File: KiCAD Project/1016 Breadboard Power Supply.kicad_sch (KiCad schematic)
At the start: 0 parts

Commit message: V1.0.0.0
Final version 1, sent for fabrication.
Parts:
- added FID1, FID2, FID3: Fiducial, Fiducial:Fiducial_1mm_Mask2mm, symbol Mechanical:Fiducial
- added H1, H2, H3, H4: MountingHole, MountingHole:MountingHole_2.1mm, symbol Mechanical:MountingHole
- added P1: DW_PCB_Logo, DW_Footprint:DW_PCB_Logo, symbol DW_Library:DW_PCB_Logo
- added P2, P3: Solder_Stencil_Alignment_Pin, DW_Footprint:Solder_Stencil_Alignment_Pin, symbol DW_Library:Solder_Stencil_Alignment_Pin
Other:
- added sheet MCU Control (MCU Control.kicad_sch)
- added sheet Rail B Power Regulator (Rail B Power Regulator.kicad_sch)
- added sheet Rail Output (Rail Output.kicad_sch)
- added sheet Rail T Power Regulator (Rail T Power Regulator.kicad_sch)
- sheet MCU Power Regulator ports: added Vmcu; removed none

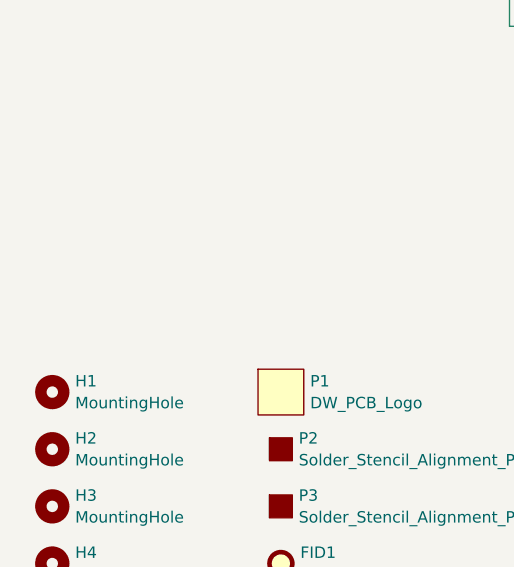
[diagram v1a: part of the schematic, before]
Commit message: v2.0.0.0
1016 Breadboard Power Supply v2

- Change FSW connection to the Vout on all regulators
- Change regulator to TPS62130A so that PG pin goes low on thermal shutdown and UVLO
- Change PG pullup to be a resistor at the regulator vice pullup within STM32 so that it can be actively discharged
- Remove resistor across rail outputs for discharging to improve efficiency
- Change board dimensions to correct span
- Change pinout of STM32 for better routing
- Change Tag-Connect footprint to momentary connection (no legs)
- Make sure Tag-Connect footprint doesn't have solder paste layer
- Added heat sinks on bottom under rail regulators, added thermal vias
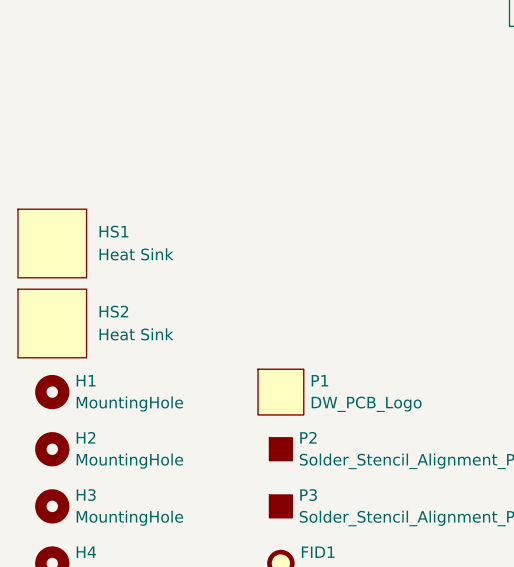
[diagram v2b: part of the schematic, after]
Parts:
- added HS1, HS2: Heat Sink, 1016:HSB01-080808, symbol 1016:HSB01-080808
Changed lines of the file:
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@@
+    )
+  )
+  (symbol (lib_id "1016:HSB01-080808") (at 38.1 148.59 0) (unit 1)
+    (in_bom yes) (on_board yes) (dnp no)
+    (property "Reference" "HS1" (at 43.18 147.32 0)
+      (effects (font (size 1.27 1.27)) (justify left))
+    )
+    (property "Value" "Heat Sink" (at 43.18 149.86 0)
+      (effects (font (size 1.27 1.27)) (justify left))
+    )
+    (property "Footprint" "1016:HSB01-080808" (at 38.1 156.21 0)
+      (effects (font (size 1.27 1.27)) hide)
+    )
+    (property "Datasheet" "https://www.mouser.com/datasheet/2/670/hsb01_080808-2449749.pdf" (at 38.1 140.97 0)
+      (effects (font (size 1.27 1.27)) hide)
+    )
+    (property "Description" "Heat Sink" (at 38.1 148.59 0)
+      (effects (font (size 1.27 1.27)) hide)
+    )
+    (property "Height" "8" (at 38.1 148.59 0)
+      (effects (font (size 1.27 1.27)) hide)
+    )
+    (property "Manufacturer_Name" "CUI Devices" (at 38.1 148.59 0)
+      (effects (font (size 1.27 1.27)) hide)
+    )
+    (property "Manufacturer_Part_Number" "HSB01-080808" (at 38.1 148.59 0)
+      (effects (font (size 1.27 1.27)) hide)
+    )
+    (property "Mouser Part Number" "490-HSB01-080808" (at 38.1 148.59 0)
+      (effects (font (size 1.27 1.27)) hide)
+    )
+    (property "Spec" "8.5mm x 8.5mm Al" (at 38.1 148.59 0)
+      (effects (font (size 1.27 1.27)) hide)
+    )
+    (instances
+      (project "1016 Breadboard Power Supply"
+        (path "/f4b22203-0926-4e3a-b453-85f22789c08a"
+          (reference "HS1") (unit 1)
+        )
+      )
+    )
+  )
+  (symbol (lib_id "1016:HSB01-080808") (at 38.1 157.48 0) (unit 1)
+    (in_bom yes) (on_board yes) (dnp no)
+    (property "Reference" "HS2" (at 43.18 156.21 0)
+      (effects (font (size 1.27 1.27)) (justify left))
+    )
+    (property "Value" "Heat Sink" (at 43.18 158.75 0)
+      (effects (font (size 1.27 1.27)) (justify left))
+    )
+    (property "Footprint" "1016:HSB01-080808" (at 38.1 165.1 0)
+      (effects (font (size 1.27 1.27)) hide)
+    )
+    (property "Datasheet" "https://www.mouser.com/datasheet/2/670/hsb01_080808-2449749.pdf" (at 38.1 149.86 0)
+      (effects (font (size 1.27 1.27)) hide)
+    )
+    (property "Description" "Heat Sink" (at 38.1 157.48 0)
+      (effects (font (size 1.27 1.27)) hide)
+    )
+    (property "Height" "8" (at 38.1 157.48 0)
+      (effects (font (size 1.27 1.27)) hide)
+    )
+    (property "Manufacturer_Name" "CUI Devices" (at 38.1 157.48 0)
+      (effects (font (size 1.27 1.27)) hide)
+    )
+    (property "Manufacturer_Part_Number" "HSB01-080808" (at 38.1 157.48 0)
+      (effects (font (size 1.27 1.27)) hide)
+    )
+    (property "Mouser Part Number" "490-HSB01-080808" (at 38.1 157.48 0)
+      (effects (font (size 1.27 1.27)) hide)
+    )
+    (property "Spec" "8.5mm x 8.5mm Al" (at 38.1 157.48 0)
+      (effects (font (size 1.27 1.27)) hide)
+    )
+    (instances
+      (project "1016 Breadboard Power Supply"
+        (path "/f4b22203-0926-4e3a-b453-85f22789c08a"
+          (reference "HS2") (unit 1)
+        )
+      )
     )
   )
